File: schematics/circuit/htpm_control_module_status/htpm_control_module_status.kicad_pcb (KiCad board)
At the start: 2 copper layers, 71.1 x 48.3 mm, 37 parts, among them J1 Conn_01x08_Socket, J2 Conn_01x04_Socket, J3 Conn_01x08_Socket

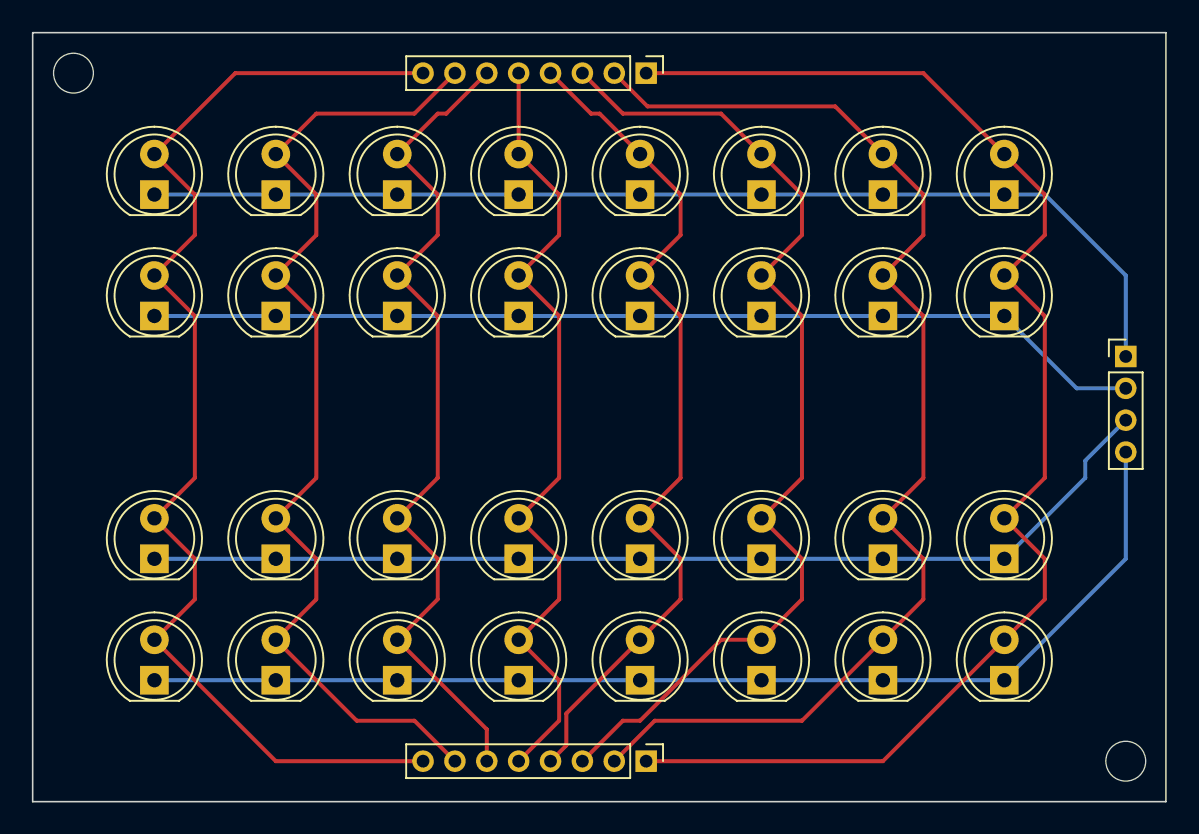
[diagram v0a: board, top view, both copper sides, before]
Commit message: Condensed HTPm CONTROL Module Status PCB.
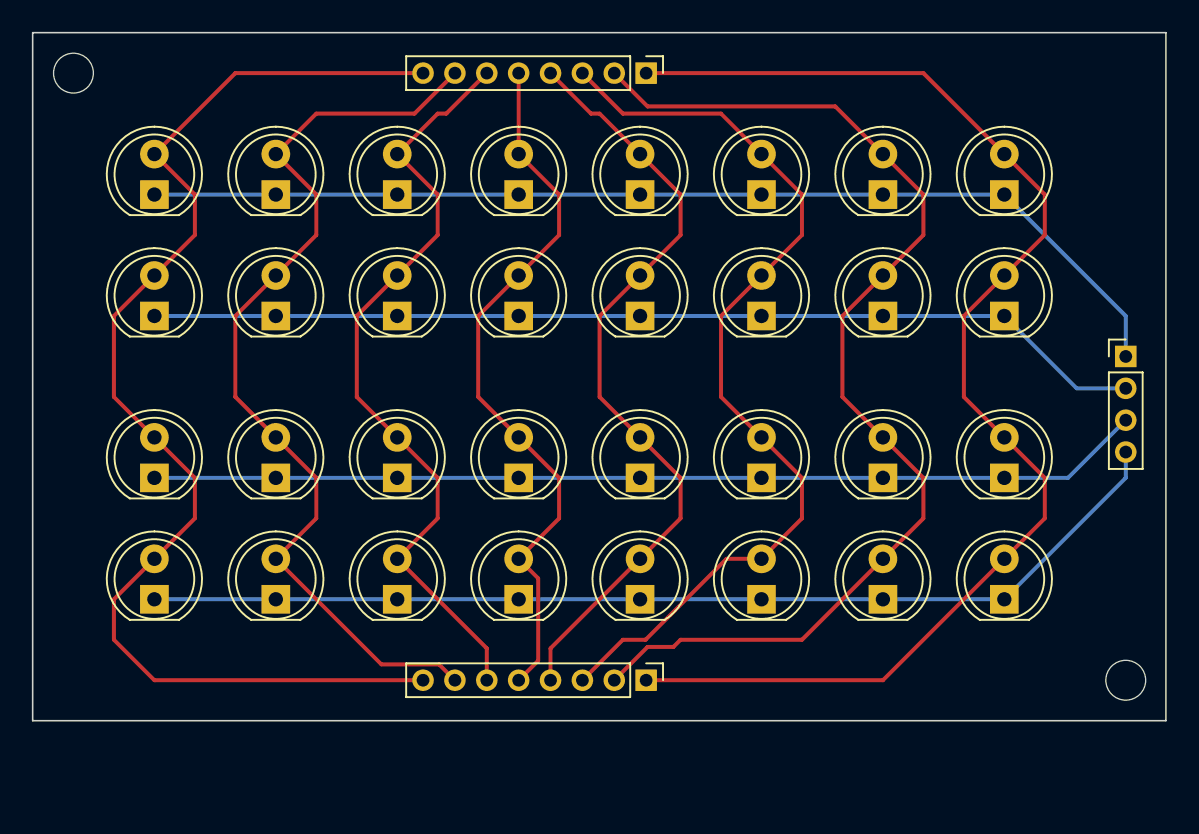
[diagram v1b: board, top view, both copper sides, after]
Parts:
- moved D17 5.08 mm to (111.8, 96.5)
- moved D18 5.08 mm to (119.4, 96.5)
- moved D19 5.08 mm to (127.0, 96.5)
- moved D20 5.08 mm to (134.6, 96.5)
- moved D21 5.08 mm to (142.2, 96.5)
- moved D22 5.08 mm to (149.9, 96.5)
- moved D23 5.08 mm to (157.5, 96.5)
- moved D24 5.08 mm to (165.1, 96.5)
- moved D25 5.08 mm to (111.8, 104.1)
- moved D26 5.08 mm to (119.4, 104.1)
- moved D27 5.08 mm to (127.0, 104.1)
- moved D28 5.08 mm to (134.6, 104.1)
- moved D29 5.08 mm to (142.2, 104.1)
- moved D30 5.08 mm to (149.9, 104.1)
- moved D31 5.08 mm to (157.5, 104.1)
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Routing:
- net Net-(D12-A): track 51.6 -> 45.4 mm
- net Net-(D15-A): track 75.8 -> 70.7 mm
- net Net-(D16-A): track 87.0 -> 81.9 mm
- net Net-(D10-A): track 64.5 -> 59.5 mm
- net Net-(D25-K): track 70.8 -> 65.7 mm
- net Net-(D11-A): track 54.5 -> 49.4 mm
- net Net-(D14-A): track 64.5 -> 59.5 mm
- net Net-(D13-A): track 54.5 -> 49.4 mm
- net Net-(D17-K): track 65.2 -> 62.5 mm
- net Net-(D1-A): track 75.8 -> 77.3 mm
- net Net-(D1-K): track 68.1 -> 66.7 mm
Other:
- board size 71.1 x 48.3 mm -> 71.1 x 43.2 mm

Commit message: Added user-facing text to HTPm CONTROL Module Status PCB.
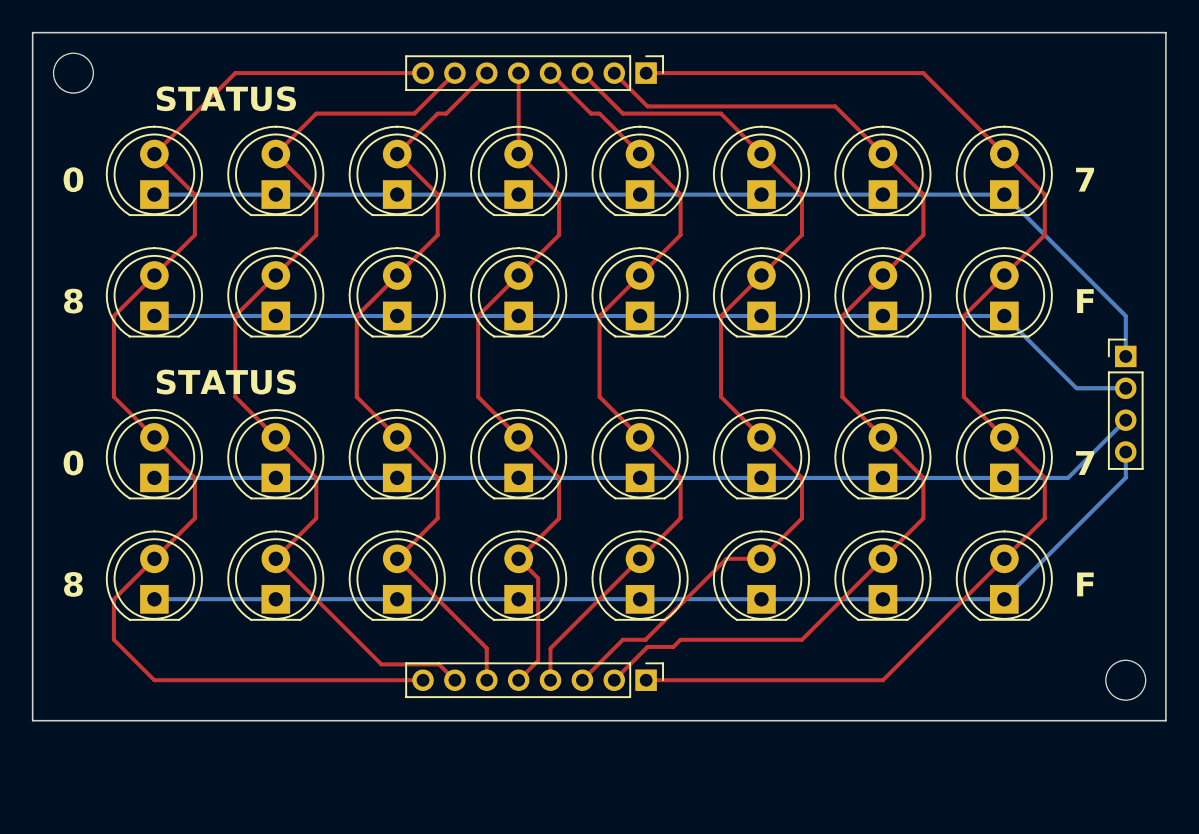
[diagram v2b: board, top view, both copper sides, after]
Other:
- board text added: "0"
- board text added: "7"
- board text added: "8"
- board text added: "F"
- board text added: "STATUS"
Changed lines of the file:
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@@
     (effects (font (size 1 1) (thickness 0.15)) (justify left bottom mirror))
+  )
+  (gr_text "0" (at 106.68 78.74) (layer "F.SilkS")
+    (effects (font (size 1.5 1.5) (thickness 0.3) bold) (justify bottom))
+  )
+  (gr_text "7" (at 170.18 78.74) (layer "F.SilkS")
+    (effects (font (size 1.5 1.5) (thickness 0.3) bold) (justify bottom))
+  )
+  (gr_text "STATUS" (at 111.76 91.44) (layer "F.SilkS")
+    (effects (font (size 1.5 1.5) (thickness 0.3) bold) (justify left bottom))
+  )
+  (gr_text "F" (at 170.18 104.14) (layer "F.SilkS")
+    (effects (font (size 1.5 1.5) (thickness 0.3) bold) (justify bottom))
+  )
+  (gr_text "7" (at 170.18 96.52) (layer "F.SilkS")
+    (effects (font (size 1.5 1.5) (thickness 0.3) bold) (justify bottom))
+  )
+  (gr_text "F" (at 170.18 86.36) (layer "F.SilkS")
+    (effects (font (size 1.5 1.5) (thickness 0.3) bold) (justify bottom))
+  )
+  (gr_text "8" (at 106.68 86.36) (layer "F.SilkS")
+    (effects (font (size 1.5 1.5) (thickness 0.3) bold) (justify bottom))
+  )
+  (gr_text "8" (at 106.68 104.14) (layer "F.SilkS")
+    (effects (font (size 1.5 1.5) (thickness 0.3) bold) (justify bottom))
+  )
+  (gr_text "STATUS" (at 111.76 73.66) (layer "F.SilkS")
+    (effects (font (size 1.5 1.5) (thickness 0.3) bold) (justify left bottom))
+  )
+  (gr_text "0" (at 106.68 96.52) (layer "F.SilkS")
+    (effects (font (size 1.5 1.5) (thickness 0.3) bold) (justify bottom))
   )
   (segment (start 165.1 78.74) (end 172.72 86.36) (width 0.25) (layer "B.Cu") (net 1))

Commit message: Updated branding on the HTPm CONTROL Module Status PCB.
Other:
- board text added: "HTP!m CONTROL"
- board text added: "Module Status"
- board text added: "by shawnd.xyz"
- board text removed: "HTP!m CONTROL Module Status"
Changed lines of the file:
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@@
   (gr_rect (start 104.12 68.58) (end 175.24 111.76)
     (stroke (width 0.1) (type default)) (fill none) (layer "Edge.Cuts"))
-  (gr_text "HTP!m CONTROL Module Status" (at 172.72 71.12) (layer "B.SilkS")
-    (effects (font (size 1 1) (thickness 0.15)) (justify left bottom mirror))
+  (gr_text "HTP!m CONTROL" (at 167.64 109.22) (layer "B.SilkS")
+    (effects (font (size 1.5 1.5) (thickness 0.3) bold) (justify left mirror))
+  )
+  (gr_text "by shawnd.xyz" (at 127 71.12) (layer "B.SilkS")
+    (effects (font (size 1.5 1.5) (thickness 0.3) bold) (justify left mirror))
+  )
+  (gr_text "Module Status" (at 162.56 71.12) (layer "B.SilkS")
+    (effects (font (size 1.5 1.5) (thickness 0.3) bold) (justify left mirror))
   )
   (gr_text "JLCJLCJLCJLC" (at 116.84 109.22) (layer "B.SilkS")
